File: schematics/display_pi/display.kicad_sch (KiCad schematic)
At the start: 4 parts, among them J1 Raspberry_Pi_4, U1 Roadside sensor, U2 Brookside sensor, U3 16x2 RGB LCD Pi Plate

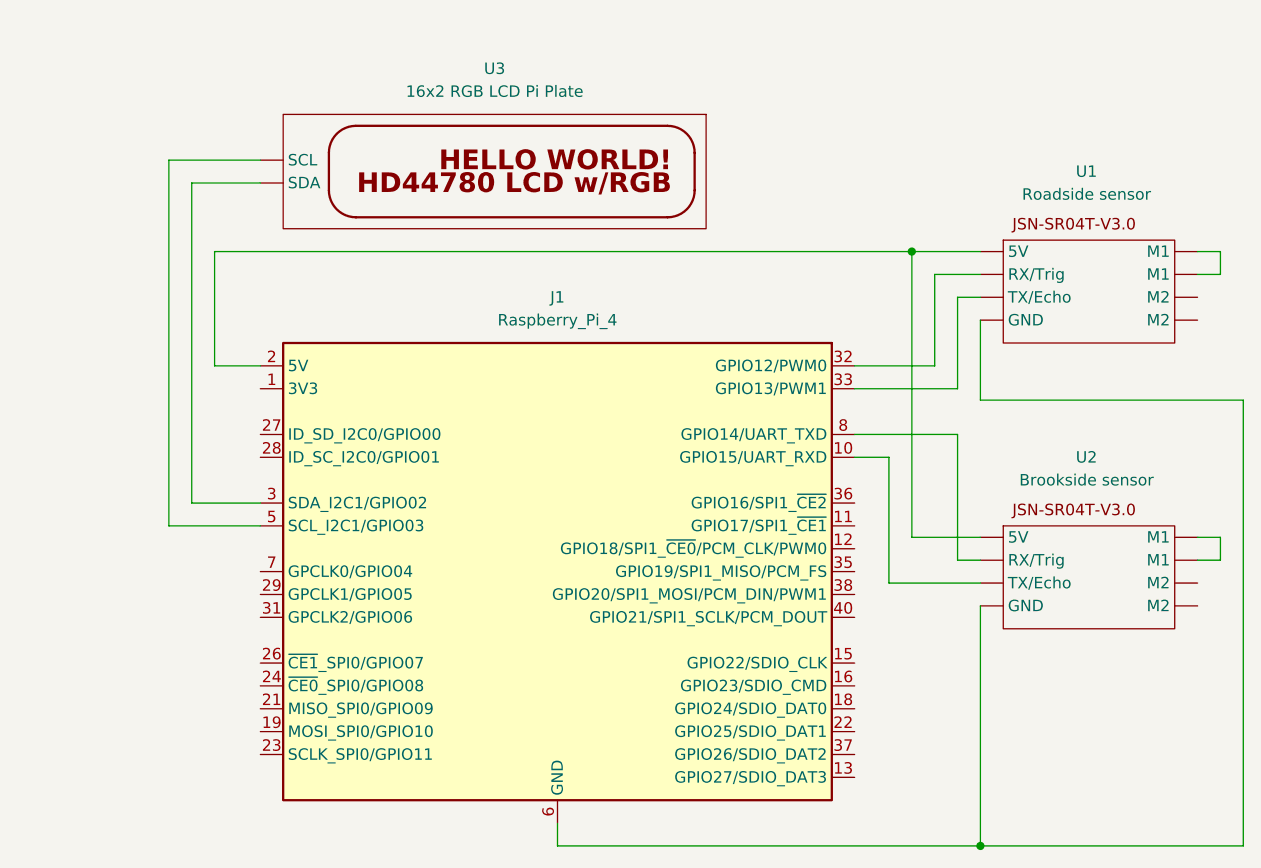
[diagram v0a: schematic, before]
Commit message: Update schematics and figures
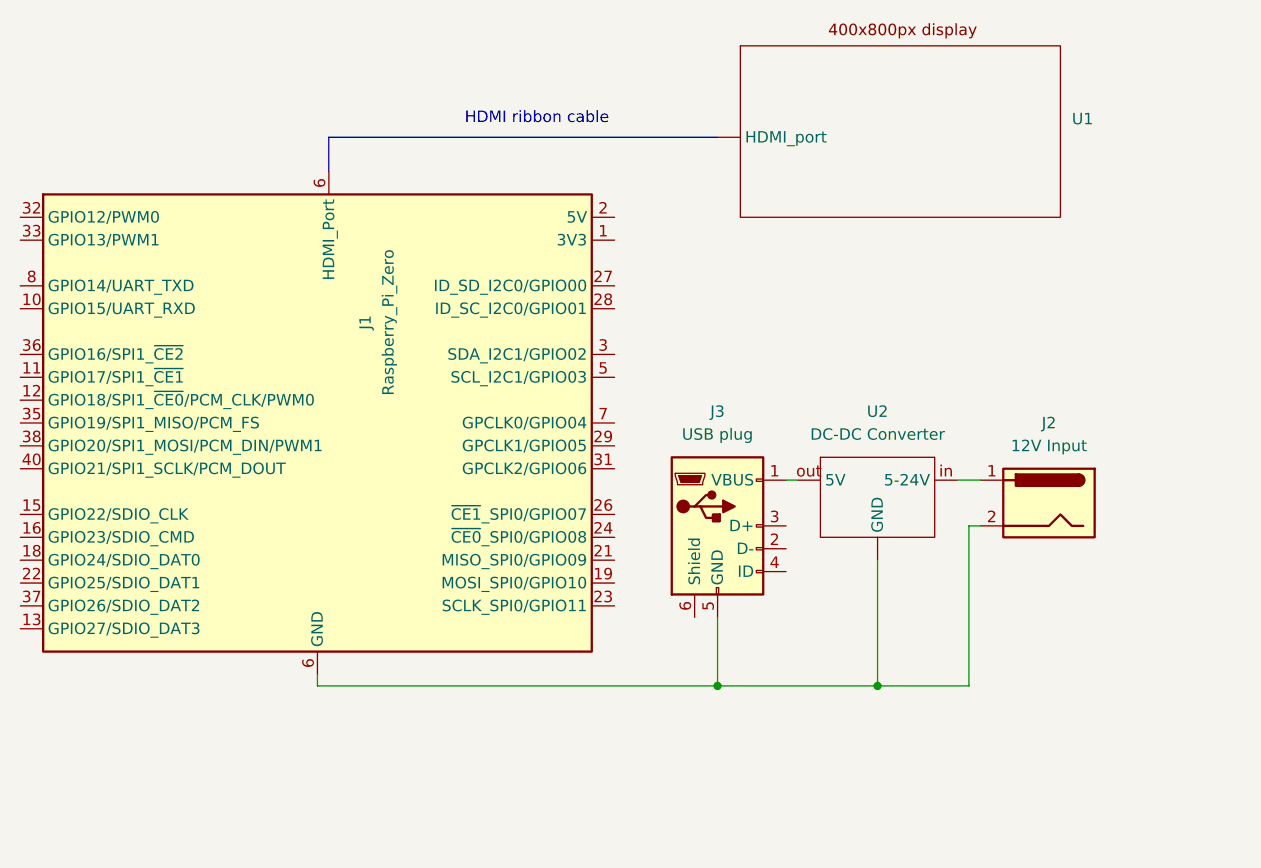
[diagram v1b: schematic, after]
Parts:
- removed U1: Roadside sensor, symbol shm_symbols:Ultrasonic_distance_sensor
- removed U2: Brookside sensor, symbol shm_symbols:Ultrasonic_distance_sensor
- removed U3: 16x2 RGB LCD Pi Plate, symbol shm_symbols:16x2_RGB_LCD_Pi_Plate
- added J2: 12V Input, symbol Connector:Barrel_Jack
- added J3: USB plug, symbol Connector:USB_B_Mini
- added U1: (no value), symbol shm_symbols:display
- added U2: DC-DC Converter, symbol shm_symbols:5V_DC-DC_converter
- J1: value Raspberry_Pi_4 -> Raspberry_Pi_Zero
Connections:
- net at J1.14 (GND), J1.20 (GND), J1.25 (GND)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: now also J2.2, J3.5 (GND), U2. (GND)
- new net: J2.1, U2.in (5-24V)
- new net: J3.1 (VBUS), U2.out (5V)
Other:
- note added: "HDMI ribbon cable"
